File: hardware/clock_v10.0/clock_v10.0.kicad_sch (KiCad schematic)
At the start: 219 parts, among them J1 RJ45, J14 DC-005B-2.5A-2.0, J2 Conn_01x03, J4 USB_C_Receptacle, J5 Conn_01x06_Pin, J8 Conn_01x02, Q1 2N7002, Q10 2N7002, Q9 2N7002, SW1 SW_Push_4PDT, U1 ADA4807-1, U10 STM32F405RGTx, U11 AMS1117-3.3, U12 BA50DD0WHFP-TR, U13 M24C02-RMN, U14 CH340C, U15 USBLC6-2P6, U16 TLV3603DCKR, U17 SN74LVC1G14DBV, U18 TMP112AIDRLR, U19 SN74LVC1G14DBV, U2 SN74LVC1G14DBV, U20 SN74LVC1G14DBV, U21 74LVC1G86, U22 74LVC1G00, U23 TPS63060, U3 SN74LVC1G14DBV, U4 ADA4807-1, U5 ADA4807-1, U6 TLV3603DCKR, U7 SN74LVC1G14DBV, U8 TLV3603DCKR, U9 L78L05_SOT89, Y1 AOCJY4A-10.000MHZ-SW, Y2 16MHz

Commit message: update reset boot on clock v10
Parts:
- removed C59: 100n, Capacitor_SMD:C_0402_1005Metric, symbol Device:C_Small
- removed R42: 330R, Resistor_SMD:R_0603_1608Metric, symbol Device:R_Small_US
- removed U21: 74LVC1G86, Package_TO_SOT_SMD:SOT-23-5, symbol 74xGxx:74LVC1G86
- removed U22: 74LVC1G00, Package_TO_SOT_SMD:SOT-23-5, symbol 74xGxx:74LVC1G00
- added TP8: ~, TestPoint:TestPoint_THTPad_D1.5mm_Drill0.7mm, symbol Connector:TestPoint
- added U21: SN74LVC1G14DBV, Package_TO_SOT_SMD:SOT-23-5, symbol 74xGxx:SN74LVC1G14DBV
- R27, R28: value 4K7 -> 47K; JLCPCB Part # C23162 -> C25819
- R31: JLCPCB Part # (none) -> C25808
- R41: value 330R -> 1K0; JLCPCB Part # C23138 -> C21190
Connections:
- net +3.3V: now also U21.5 (VCC)
- net GND: now also U21.3 (GND)
- net USB_DTR: now also JP1.1 (A)
- net USB_RTS: now also TP8.1, U21.2
- net at R41.1: now also U21.4
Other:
- note added: "TODO - set reg voltage FB will 0.5V Currently set about 6.0 V"
- note removed: "TODO - set reg voltage FB will 0.5V Currnently set about 6.0 V"
- moved on the sheet: C27, C33, C34, C37, C39, C41, C42, C44, C58, C60, C61, C62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

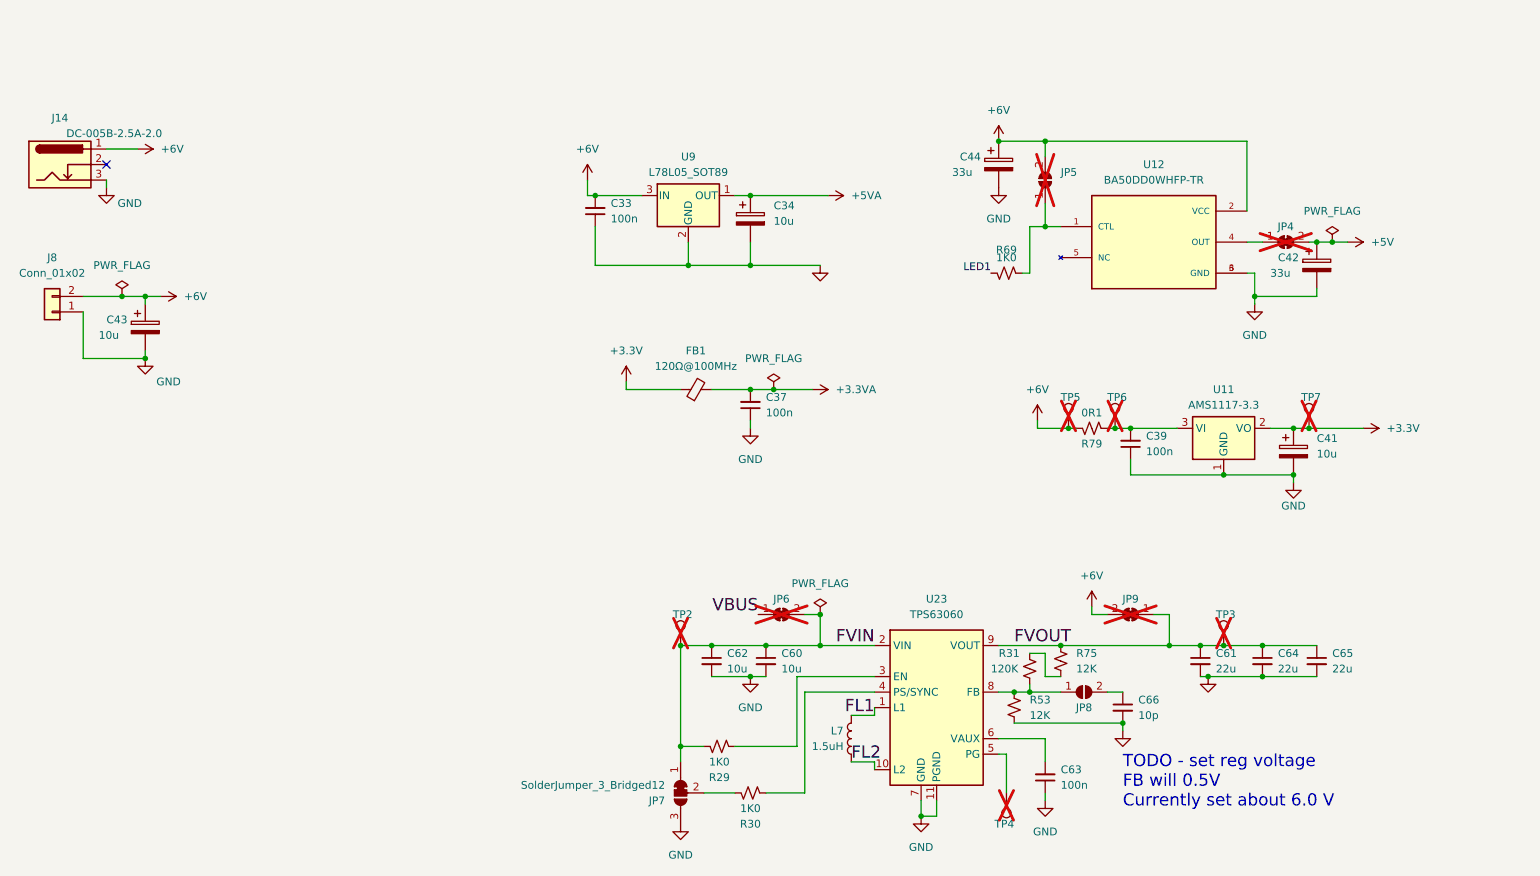
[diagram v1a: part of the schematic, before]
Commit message: fix up ground on clock v10
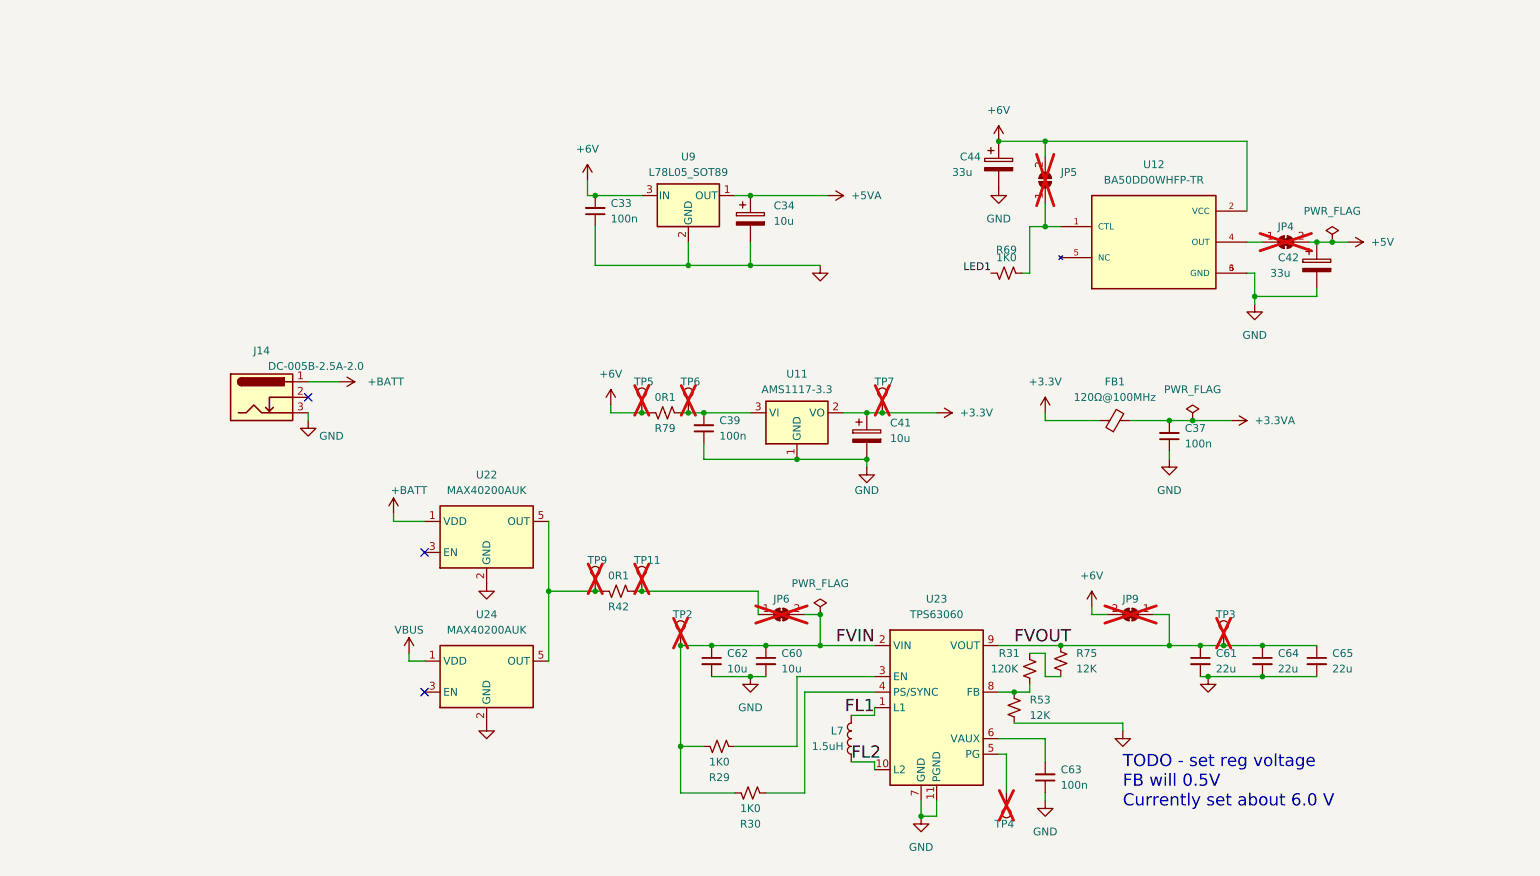
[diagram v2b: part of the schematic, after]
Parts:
- removed C43: 10u, Capacitor_Tantalum_SMD:CP_EIA-3216-18_Kemet-A, symbol Device:C_Polarized
- removed C66: 10p, Capacitor_SMD:C_0603_1608Metric, symbol Device:C_Small
- removed J8: Conn_01x02, Connector_JST:JST_PH_S2B-PH-SM4-TB_1x02-1MP_P2.00mm_Horizontal, symbol Connector_Generic:Conn_01x02
- removed JP7: SolderJumper_3_Bridged12, Jumper:SolderJumper-3_P1.3mm_Bridged2Bar12_RoundedPad1.0x1.5mm, symbol Jumper:SolderJumper_3_Bridged12
- removed JP8: SolderJumper_2_Open, Jumper:SolderJumper-2_P1.3mm_Open_RoundedPad1.0x1.5mm, symbol Jumper:SolderJumper_2_Open
- added R42: 0R1, Resistor_SMD:R_1206_3216Metric, symbol Device:R_Small_US
- added TP11, TP9: ~, TestPoint:TestPoint_THTPad_D1.0mm_Drill0.5mm, symbol Connector:TestPoint
- added U22, U24: MAX40200AUK, Package_TO_SOT_SMD:SOT-23-5, symbol Analog_Switch:MAX40200AUK
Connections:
- net +6V: no longer J14.1
- net FVIN: now also R30.1
- net GND: now also U22.2 (GND), U24.2 (GND)
- net VBUS: now also U24.1 (VDD); no longer JP6.1 (A)
- new net: JP6.1 (A), R42.1, TP11.1
- new net: R42.2, TP9.1, U22.5 (OUT), U24.5 (OUT)
- new net +BATT: J14.1, U22.1 (VDD)
- no-connect marks 30 -> 32
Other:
- moved on the sheet: C37, C39, C41, FB1, J14, R79, TP5, TP6, TP7, U11

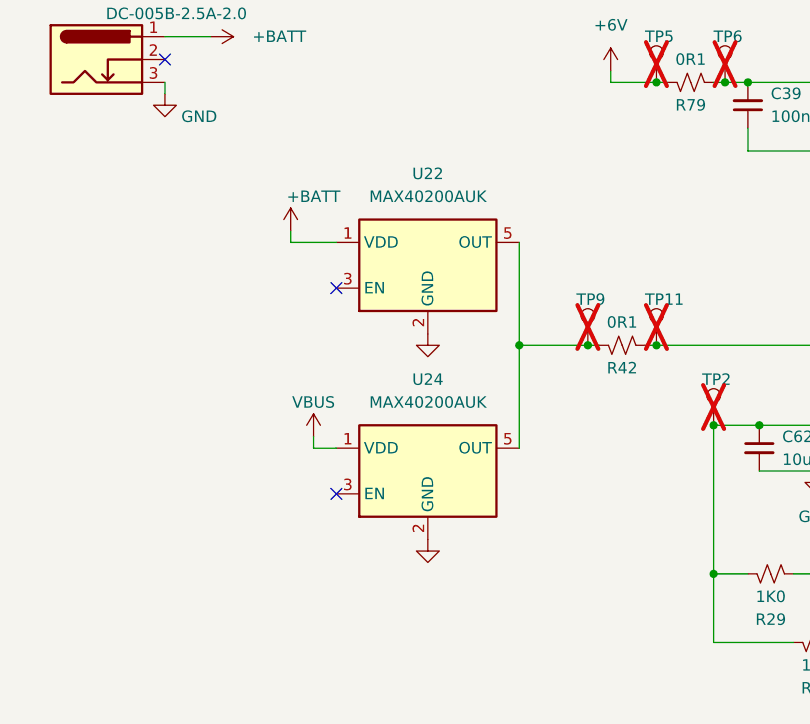
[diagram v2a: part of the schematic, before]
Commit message: update diodes on clock board
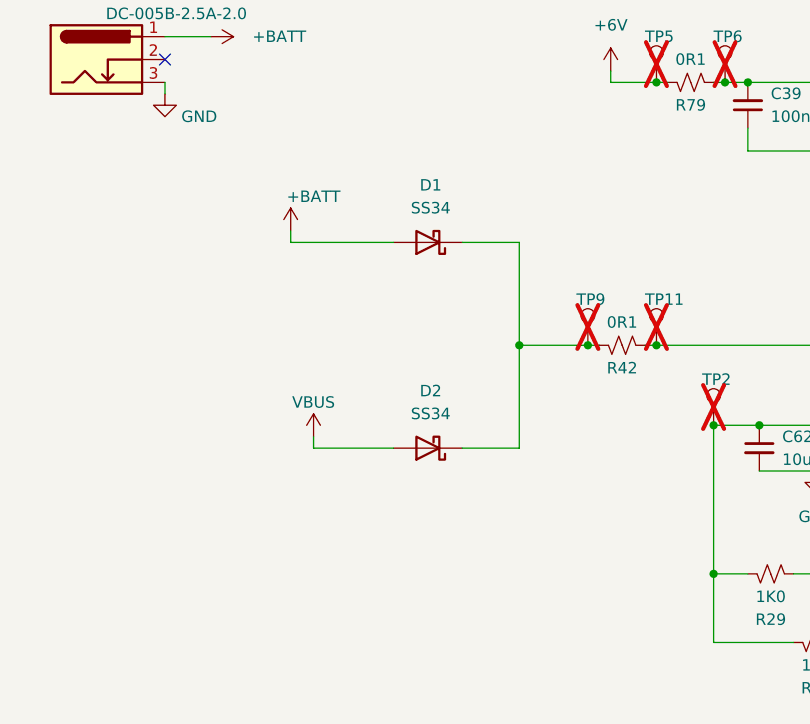
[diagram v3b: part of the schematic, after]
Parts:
- removed U22, U24: MAX40200AUK, Package_TO_SOT_SMD:SOT-23-5, symbol Analog_Switch:MAX40200AUK
- added D1, D2: SS34, Diode_SMD:D_SMA, symbol Diode:MBRA340
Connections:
- net +BATT: now also D1.2 (A)
- net VBUS: now also D2.2 (A)
- net at R42.2, TP9.1: now also D1.1 (K), D2.1 (K)
- no-connect marks 32 -> 30
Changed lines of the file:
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@@
   (no_connect (at 177.8 93.98))
   (no_connect (at 177.8 86.36))
-  (no_connect (at 88.9 379.73))
   (no_connect (at 276.86 41.91))
   (no_connect (at 177.8 63.5))
@@
   (no_connect (at 276.86 49.53))
   (no_connect (at 177.8 78.74))
-  (no_connect (at 88.9 356.87))
   (no_connect (at 177.8 73.66))
   (no_connect (at 177.8 60.96))
@@
     (stroke (width 0) (type default))
   )
+  (wire (pts (xy 102.87 351.79) (xy 109.22 351.79))
+    (stroke (width 0) (type default))
+  )
   (wire (pts (xy 181.61 256.54) (xy 177.8 256.54))
     (stroke (width 0) (type default))
@@
     (stroke (width 0) (type default))
   )
+  (wire (pts (xy 102.87 374.65) (xy 109.22 374.65))
+    (stroke (width 0) (type default))
+  )
   (wire (pts (xy 326.39 222.25) (xy 328.93 222.25))
     (stroke (width 0) (type default))
@@
     (stroke (width 0) (type default))
   )
-  (wire (pts (xy 88.9 351.79) (xy 83.82 351.79))
+  (wire (pts (xy 83.82 351.79) (xy 95.25 351.79))
     (stroke (width 0) (type default))
   )
@@
     (stroke (width 0) (type default))
   )
-  (wire (pts (xy 88.9 374.65) (xy 86.36 374.65))
+  (wire (pts (xy 86.36 374.65) (xy 95.25 374.65))
     (stroke (width 0) (type default))
   )
@@
     )
   )
+  (symbol (lib_id "Diode:MBRA340") (at 99.06 374.65 180) (unit 1)
+    (in_bom yes) (on_board yes) (dnp no) (fields_autoplaced)
+    (property "Reference" "D2" (at 99.3775 368.3 0)
+      (effects (font (size 1.27 1.27)))
+    )
+    (property "Value" "SS34" (at 99.3775 370.84 0)
+      (effects (font (size 1.27 1.27)))
+    )
+    (property "Footprint" "Diode_SMD:D_SMA" (at 99.06 370.205 0)
+      (effects (font (size 1.27 1.27)) hide)
+    )
+    (property "Datasheet" "" (at 99.06 374.65 0)
+      (effects (font (size 1.27 1.27)) hide)
+    )
+    (property "JLCPCB Part #" "C8678" (at 99.06 374.65 0)
+      (effects (font (size 1.27 1.27)) hide)
+    )
+    (property "MANUFACTURER" "MDD" (at 99.06 374.65 0)
+      (effects (font (size 1.27 1.27)) hide)
+    )
+    (property "MPN" "SS34" (at 99.06 374.65 0)
+      (effects (font (size 1.27 1.27)) hide)
+    )
+    (pin "1")
+    (pin "2")
+    (instances
+      (project "clock_v10.0"
+        (path "/bd4d3b9a-07c1-4a53-9c94-2893f3e869d4"
+          (reference "D2") (unit 1)
+        )
+      )
+    )
+  )
   (symbol (lib_id "BlinkyShared:147873-2") (at 436.88 262.89 0) (unit 1)
     (in_bom yes) (on_board yes) (dnp no) (fields_autoplaced)
@@
     )
   )
-  (symbol (lib_id "power:GND") (at 99.06 361.95 0) (unit 1)
-    (in_bom yes) (on_board yes) (dnp no)
-    (property "Reference" "#PWR0137" (at 99.06 368.3 0)
-      (effects (font (size 1.27 1.27)) hide)
-    )
-    (property "Value" "GND" (at 99.06 367.03 0)
-      (effects (font (size 1.27 1.27)) hide)
-    )
-    (property "Footprint" "" (at 99.06 361.95 0)
-      (effects (font (size 1.27 1.27)) hide)
-    )
-    (property "Datasheet" "" (at 99.06 361.95 0)
-      (effects (font (size 1.27 1.27)) hide)
-    )
-    (pin "1")
-    (instances
-      (project "clock_v10.0"
-        (path "/bd4d3b9a-07c1-4a53-9c94-2893f3e869d4"
-          (reference "#PWR0137") (unit 1)
-        )
-      )
-    )
-  )
   (symbol (lib_id "power:GND") (at 283.21 22.86 0) (mirror y) (unit 1)
     (in_bom yes) (on_board yes) (dnp no)
@@
     )
   )
-  (symbol (lib_id "Analog_Switch:MAX40200AUK") (at 99.06 354.33 0) (unit 1)
-    (in_bom yes) (on_board yes) (dnp no) (fields_autoplaced)
-    (property "Reference" "U22" (at 99.06 344.17 0)
-      (effects (font (size 1.27 1.27)))
-    )
-    (property "Value" "MAX40200AUK" (at 99.06 346.71 0)
-      (effects (font (size 1.27 1.27)))
-    )
-    (property "Footprint" "Package_TO_SOT_SMD:SOT-23-5" (at 99.06 341.63 0)
-      (effects (font (size 1.27 1.27)) hide)
-    )
-    (property "Datasheet" "https://datasheets.maximintegrated.com/en/ds/MAX40200.pdf" (at 99.06 341.63 0)
-      (effects (font (size 1.27 1.27)) hide)
-    )
-    (property "JLCPCB Part #" "C2649430" (at 99.06 354.33 0)
-      (effects (font (size 1.27 1.27)) hide)
-    )
-    (pin "1")
-    (pin "2")
-    (pin "3")
-    (pin "4")
-    (pin "5")
-    (instances
-      (project "clock_v10.0"
-        (path "/bd4d3b9a-07c1-4a53-9c94-2893f3e869d4"
-          (reference "U22") (unit 1)
-        )
-      )
-    )
-  )
   (symbol (lib_id "Device:R_Small_US") (at 256.54 254 0) (unit 1)
     (in_bom yes) (on_board yes) (dnp no) (fields_autoplaced)
@@
     )
   )
-  (symbol (lib_id "Analog_Switch:MAX40200AUK") (at 99.06 377.19 0) (unit 1)
-    (in_bom yes) (on_board yes) (dnp no) (fields_autoplaced)
-    (property "Reference" "U24" (at 99.06 367.03 0)
-      (effects (font (size 1.27 1.27)))
-    )
-    (property "Value" "MAX40200AUK" (at 99.06 369.57 0)
-      (effects (font (size 1.27 1.27)))
-    )
-    (property "Footprint" "Package_TO_SOT_SMD:SOT-23-5" (at 99.06 364.49 0)
-      (effects (font (size 1.27 1.27)) hide)
-    )
-    (property "Datasheet" "https://datasheets.maximintegrated.com/en/ds/MAX40200.pdf" (at 99.06 364.49 0)
-      (effects (font (size 1.27 1.27)) hide)
-    )
-    (property "JLCPCB Part #" "C2649430" (at 99.06 377.19 0)
-      (effects (font (size 1.27 1.27)) hide)
-    )
-    (pin "1")
-    (pin "2")
-    (pin "3")
-    (pin "4")
-    (pin "5")
-    (instances
-      (project "clock_v10.0"
-        (path "/bd4d3b9a-07c1-4a53-9c94-2893f3e869d4"
-          (reference "U24") (unit 1)
-        )
-      )
-    )
-  )
   (symbol (lib_id "power:+3.3VA") (at 271.78 224.79 0) (unit 1)
     (in_bom yes) (on_board yes) (dnp no) (fields_autoplaced)
@@
     )
   )
-  (symbol (lib_id "power:GND") (at 99.06 384.81 0) (unit 1)
-    (in_bom yes) (on_board yes) (dnp no)
-    (property "Reference" "#PWR0139" (at 99.06 391.16 0)
-      (effects (font (size 1.27 1.27)) hide)
-    )
-    (property "Value" "GND" (at 99.06 389.89 0)
-      (effects (font (size 1.27 1.27)) hide)
-    )
-    (property "Footprint" "" (at 99.06 384.81 0)
-      (effects (font (size 1.27 1.27)) hide)
-    )
-    (property "Datasheet" "" (at 99.06 384.81 0)
-      (effects (font (size 1.27 1.27)) hide)
-    )
-    (pin "1")
-    (instances
-      (project "clock_v10.0"
-        (path "/bd4d3b9a-07c1-4a53-9c94-2893f3e869d4"
-          (reference "#PWR0139") (unit 1)
-        )
-      )
-    )
-  )
   (symbol (lib_id "power:+5VA") (at 342.9 96.52 0) (unit 1)
     (in_bom yes) (on_board yes) (dnp no)
@@
         )
       )
+    )
+  )
+  (symbol (lib_id "Diode:MBRA340") (at 99.06 351.79 180) (unit 1)
+    (in_bom yes) (on_board yes) (dnp no) (fields_autoplaced)
+    (property "Reference" "D1" (at 99.3775 345.44 0)
+      (effects (font (size 1.27 1.27)))
+    )
+    (property "Value" "SS34" (at 99.3775 347.98 0)
+      (effects (font (size 1.27 1.27)))
+    )
+    (property "Footprint" "Diode_SMD:D_SMA" (at 99.06 347.345 0)
+      (effects (font (size 1.27 1.27)) hide)
+    )
+    (property "Datasheet" "" (at 99.06 351.79 0)
+      (effects (font (size 1.27 1.27)) hide)
+    )
+    (property "JLCPCB Part #" "C8678" (at 99.06 351.79 0)
+      (effects (font (size 1.27 1.27)) hide)
+    )
+    (property "MANUFACTURER" "MDD" (at 99.06 351.79 0)
+      (effects (font (size 1.27 1.27)) hide)
+    )
+    (property "MPN" "SS34" (at 99.06 351.79 0)
+      (effects (font (size 1.27 1.27)) hide)
+    )
+    (pin "1")
+    (pin "2")
+    (instances
+      (project "clock_v10.0"
+        (path "/bd4d3b9a-07c1-4a53-9c94-2893f3e869d4"
+          (reference "D1") (unit 1)
+        )
+      )
